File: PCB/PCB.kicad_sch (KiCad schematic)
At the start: 9 parts, among them U1 STM8S003F3P, U2 PCB-USB-PWR-connector, U3 D168K

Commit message: Reflect MCU on dev board with original pinout
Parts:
- U1: value STM8S003F3P -> STM8S103F3P
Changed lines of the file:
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@@
       (effects (font (size 1.27 1.27)) (justify left))
     )
-    (property "Value" "STM8S003F3P" (id 1) (at 103.505 123.19 0)
+    (property "Value" "STM8S103F3P" (id 1) (at 103.505 123.19 0)
       (effects (font (size 1.27 1.27)) (justify left))
     )
@@
       (effects (font (size 1.27 1.27)) (justify left) hide)
     )
-    (property "Datasheet" "http://www.st.com/st-web-ui/static/active/en/resource/technical/document/datasheet/DM00024550.pdf" (id 3) (at 101.6 110.49 0)
+    (property "Datasheet" "https://www.st.com/content/ccc/resource/technical/document/datasheet/ce/13/13/03/a9/a4/42/8f/CD00226640.pdf/files/CD00226640.pdf/jcr:content/translations/en.CD00226640.pdf" (id 3) (at 101.6 110.49 0)
       (effects (font (size 1.27 1.27)) hide)
     )
@@
     )
     (path "/a60cc657-38f8-45b9-8ac4-f9d708d9d5b2"
-      (reference "U1") (unit 1) (value "STM8S003F3P") (footprint "Package_SO:TSSOP-20_4.4x6.5mm_P0.65mm")
+      (reference "U1") (unit 1) (value "STM8S103F3P") (footprint "Package_SO:TSSOP-20_4.4x6.5mm_P0.65mm")
     )
     (path "/a0e74fdd-2272-42b1-9d9a-65553efcd00a"

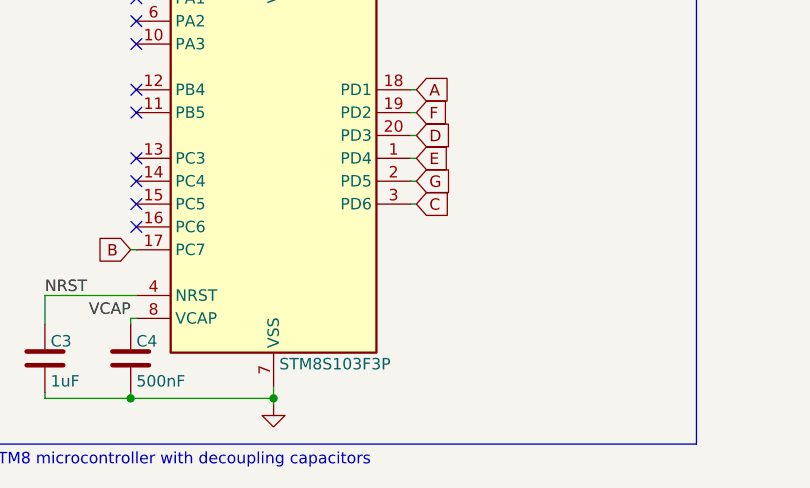
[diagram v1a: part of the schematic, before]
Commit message: Add UART header
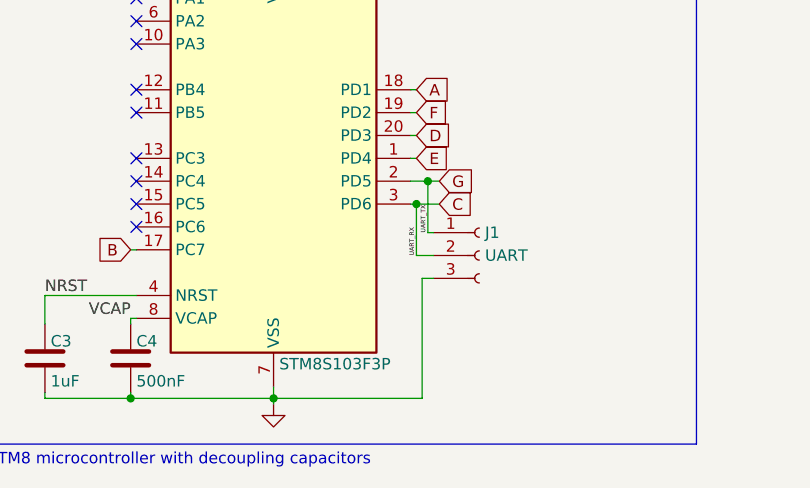
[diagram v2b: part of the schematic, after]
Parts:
- added J1: UART, Connector:FanPinHeader_1x03_P2.54mm_Vertical, symbol Connector:Conn_01x03_Female
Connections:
- net C: now also J1.2 (Pin_2)
- net G: now also J1.1 (Pin_1)
- net GND: now also J1.3 (Pin_3)
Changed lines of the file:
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@@
     (company "Johnathan Trachte")
+  )
+  (junction (at 118.745 105.41) (diameter 0) (color 0 0 0 0)
+  )
+  (junction (at 120.015 102.87) (diameter 0) (color 0 0 0 0)
   )
   (junction (at 86.995 127) (diameter 0) (color 0 0 0 0)
@@
   (no_connect (at 87.63 92.71))
   (no_connect (at 87.63 95.25))
+  (wire (pts (xy 118.745 105.41) (xy 121.285 105.41))
+    (stroke (width 0) (type default) (color 0 0 0 0))
+  )
   (polyline (pts (xy 218.44 69.85) (xy 254.635 69.85))
     (stroke (width 0) (type default) (color 0 0 0 0))
@@
     (stroke (width 0) (type default) (color 0 0 0 0))
   )
+  (wire (pts (xy 120.65 108.585) (xy 120.015 108.585))
+    (stroke (width 0) (type default) (color 0 0 0 0))
+  )
   (wire (pts (xy 241.935 95.885) (xy 242.57 95.885))
     (stroke (width 0) (type default) (color 0 0 0 0))
@@
     (stroke (width 0) (type default) (color 0 0 0 0))
   )
+  (wire (pts (xy 119.38 113.665) (xy 120.65 113.665))
+    (stroke (width 0) (type default) (color 0 0 0 0))
+  )
   (wire (pts (xy 111.125 65.405) (xy 111.125 66.04))
     (stroke (width 0) (type default) (color 0 0 0 0))
@@
     (stroke (width 0) (type default) (color 0 0 0 0))
   )
-  (wire (pts (xy 118.745 102.87) (xy 118.11 102.87))
+  (wire (pts (xy 118.11 102.87) (xy 120.015 102.87))
     (stroke (width 0) (type default) (color 0 0 0 0))
   )
@@
     (stroke (width 0) (type default) (color 0 0 0 0))
   )
+  (wire (pts (xy 119.38 127) (xy 102.87 127))
+    (stroke (width 0) (type default) (color 0 0 0 0))
+  )
   (wire (pts (xy 85.09 66.04) (xy 95.25 66.04))
     (stroke (width 0) (type default) (color 0 0 0 0))
@@
     (stroke (width 0) (type default) (color 0 0 0 0))
   )
+  (wire (pts (xy 118.745 111.125) (xy 120.65 111.125))
+    (stroke (width 0) (type default) (color 0 0 0 0))
+  )
+  (wire (pts (xy 120.015 108.585) (xy 120.015 102.87))
+    (stroke (width 0) (type default) (color 0 0 0 0))
+  )
   (wire (pts (xy 118.745 92.71) (xy 118.11 92.71))
     (stroke (width 0) (type default) (color 0 0 0 0))
@@
     (stroke (width 0) (type default) (color 0 0 0 0))
   )
+  (wire (pts (xy 120.015 102.87) (xy 121.285 102.87))
+    (stroke (width 0) (type default) (color 0 0 0 0))
+  )
+  (wire (pts (xy 118.745 105.41) (xy 118.745 111.125))
+    (stroke (width 0) (type default) (color 0 0 0 0))
+  )
   (wire (pts (xy 111.125 66.04) (xy 120.015 66.04))
     (stroke (width 0) (type default) (color 0 0 0 0))
@@
   )
   (wire (pts (xy 102.87 127) (xy 102.87 127.635))
+    (stroke (width 0) (type default) (color 0 0 0 0))
+  )
+  (wire (pts (xy 119.38 113.665) (xy 119.38 127))
     (stroke (width 0) (type default) (color 0 0 0 0))
   )
@@
   (text "8-segment display with pull-down resistors" (at 218.44 112.395 0)
     (effects (font (size 1.27 1.27)) (justify left bottom))
+  )
+  (label "UART_RX" (at 118.745 111.125 90)
+    (effects (font (size 0.5 0.5)) (justify left bottom))
+  )
+  (label "UART_TX" (at 120.015 108.585 90)
+    (effects (font (size 0.5 0.5)) (justify left bottom))
   )
   (label "VCAP" (at 86.995 118.11 180)
@@
     )
   )
-  (global_label "G" (shape input) (at 118.745 102.87 0) (fields_autoplaced)
+  (global_label "G" (shape input) (at 121.285 102.87 0) (fields_autoplaced)
     (effects (font (size 1.27 1.27)) (justify left))
-    (property "Intersheet References" "${INTERSHEET_REFS}" (id 0) (at 122.4281 102.7906 0)
+    (property "Intersheet References" "${INTERSHEET_REFS}" (id 0) (at 124.9681 102.7906 0)
       (effects (font (size 1.27 1.27)) (justify left) hide)
     )
@@
     )
   )
-  (global_label "C" (shape input) (at 118.745 105.41 0) (fields_autoplaced)
+  (global_label "C" (shape input) (at 121.285 105.41 0) (fields_autoplaced)
     (effects (font (size 1.27 1.27)) (justify left))
-    (property "Intersheet References" "${INTERSHEET_REFS}" (id 0) (at 122.4281 105.3306 0)
+    (property "Intersheet References" "${INTERSHEET_REFS}" (id 0) (at 124.9681 105.3306 0)
       (effects (font (size 1.27 1.27)) (justify left) hide)
     )
@@
     (pin "1")
     (pin "2")
+  )
+  (symbol (lib_id "Connector:Conn_01x03_Female") (at 125.73 111.125 0) (unit 1)
+    (in_bom yes) (on_board yes)
+    (property "Reference" "J1" (id 0) (at 126.365 108.585 0)
+      (effects (font (size 1.27 1.27)) (justify left))
+    )
+    (property "Value" "UART" (id 1) (at 126.365 111.125 0)
+      (effects (font (size 1.27 1.27)) (justify left))
+    )
+    (property "Footprint" "Connector:FanPinHeader_1x03_P2.54mm_Vertical" (id 2) (at 125.73 111.125 0)
+      (effects (font (size 1.27 1.27)) hide)
+    )
+    (property "Datasheet" "~" (id 3) (at 125.73 111.125 0)
+      (effects (font (size 1.27 1.27)) hide)
+    )
+    (pin "1")
+    (pin "2")
+    (pin "3")
   )
   (symbol (lib_id "PCB-USB:PCB-USB-PWR-connector") (at 121.285 72.39 0) (mirror x) (unit 1)
@@
       (reference "C4") (unit 1) (value "500nF") (footprint "Capacitor_SMD:C_0805_2012Metric")
     )
+    (path "/9a5fd4ec-6e7a-49cc-a40e-d6c92b4c48b2"
+      (reference "J1") (unit 1) (value "UART") (footprint "Connector:FanPinHeader_1x03_P2.54mm_Vertical")
+    )
     (path "/95185761-cc93-45b4-82ec-42ce3d7830c2"
